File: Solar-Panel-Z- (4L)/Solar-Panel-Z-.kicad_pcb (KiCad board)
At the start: 4 copper layers, 48.4 x 48.4 mm, 81 parts, among them J1 FTS-105-01-L-DV-A, Q1 BSS138DWQ-7, Q2 MBT2222ADW1T1, Q3 BSS138DWQ-7, Q4 MBT2222ADW1T1, U1 BQ25570RGRR, U2 TSL2561

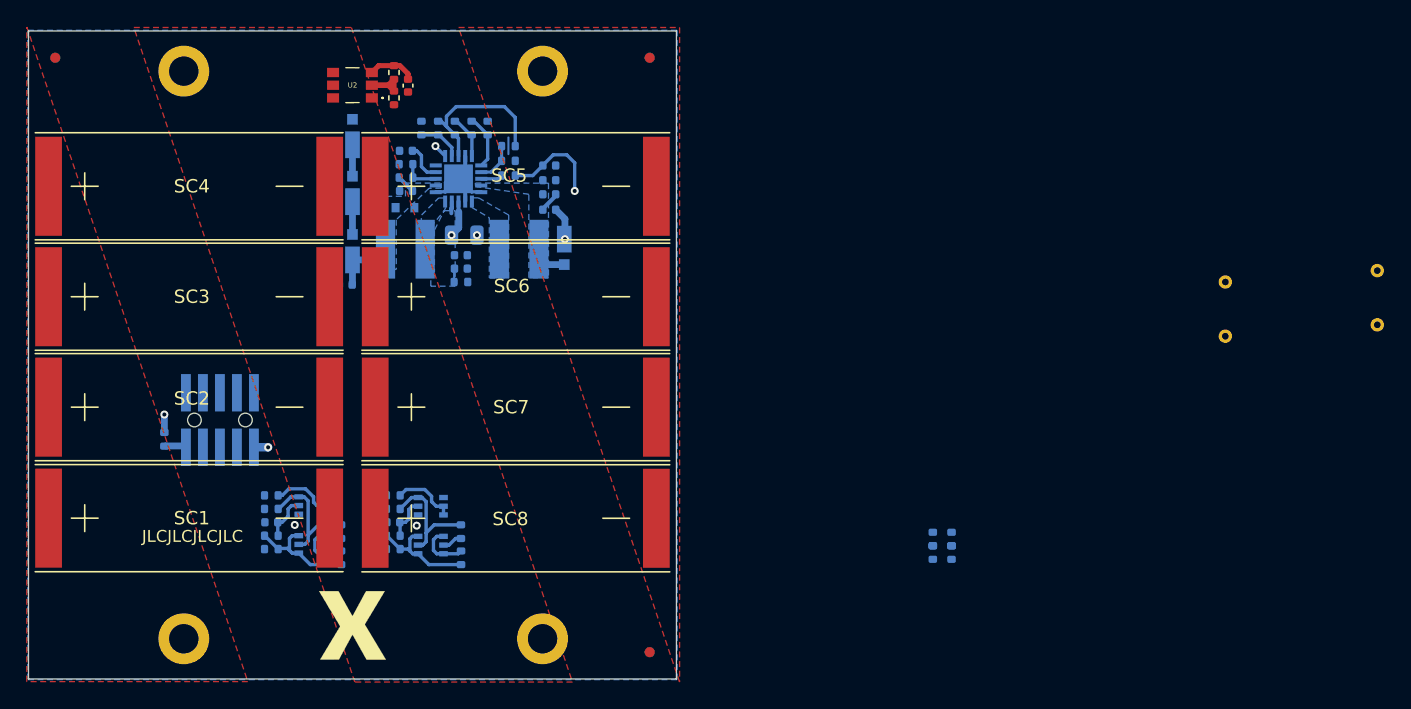
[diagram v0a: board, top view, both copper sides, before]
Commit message: Added 4 Layer Z- board
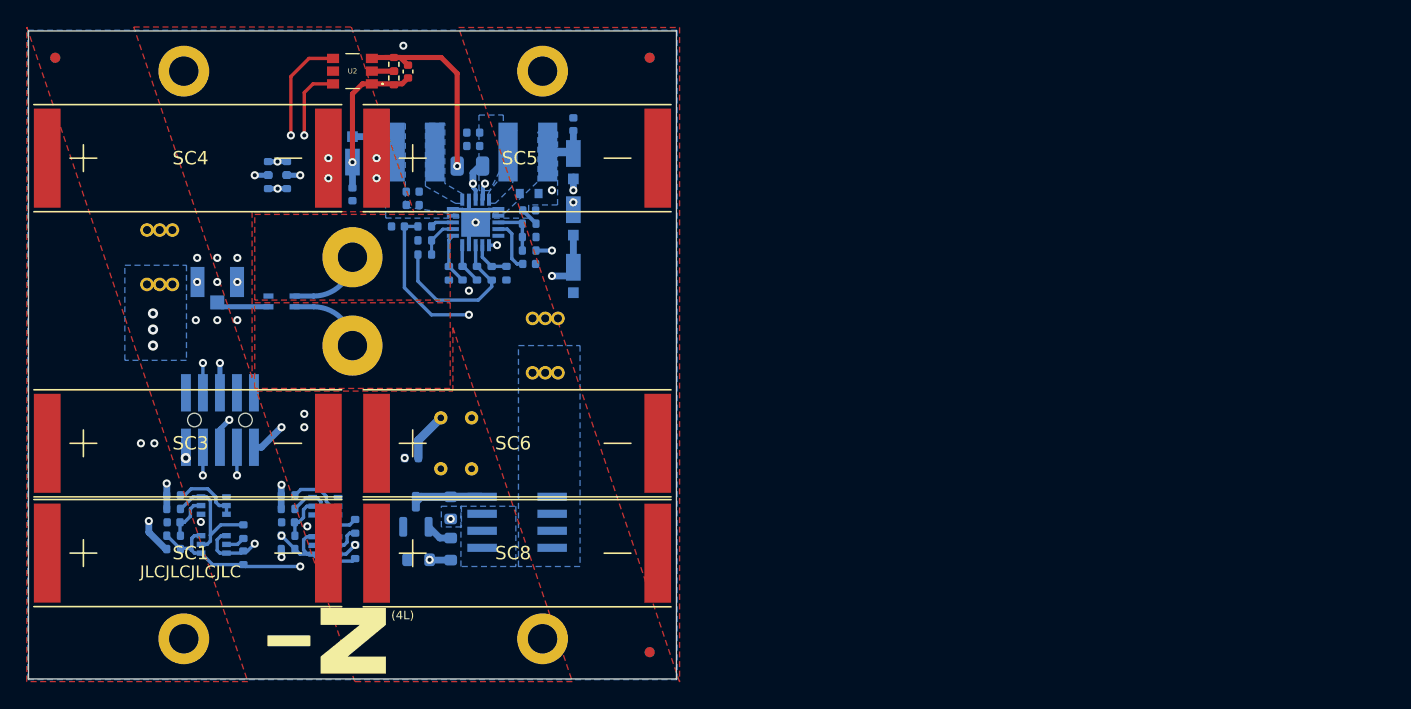
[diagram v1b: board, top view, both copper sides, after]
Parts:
- removed the REF** at (106.7, 88.2)
- removed SC2, SC7: SolarCell_Small, solarpanels:KXOB25-05X3F
- added H5: MountingHole_Pad, solarpanels:Antenna Pad, F.Cu at (106.7, 59.2)
- added H6: MountingHole_Pad, solarpanels:Antenna Pad, F.Cu at (106.7, 65.8)
- added J2: U.FL-R-SMT-1, solarpanels:U.FL-R-SMT-1, B.Cu at (96.6, 61.0)
- added JP1: Jumper, solarpanels:Burn-Wire-Rotated, B.Cu at (92.3, 59.2)
- added JP2: Jumper, solarpanels:Burn-Wire-Rotated, B.Cu at (121.1, 65.8)
- added Q5: IRLML2803, Package_TO_SOT_SMD:SOT-23, B.Cu at (111.4, 78.4)
- added R32: 4.7k, Resistor_SMD:R_0603_1608Metric, B.Cu at (114.0, 81.0)
- added R33: 100k, Resistor_SMD:R_0603_1608Metric, B.Cu at (114.0, 77.9)
- added R4: 10k, Resistor_SMD:R_0603_1608Metric, B.Cu at (111.6, 81.8)
- added Ref**: Val**, custom-footprints:ypanel, F.Cu at (106.1, 87.6)
- added U3: ATB2012-50011-T000, solarpanels:ATB2012, B.Cu at (101.4, 62.5)
- added U4: NDS8434, solarpanels:NDS8434, B.Cu at (119.0, 79.0)
- moved TP4 70.3 mm to (113.3, 71.2)
- moved TP3 69.3 mm to (115.6, 75.0)
- moved TP2 59.4 mm to (113.3, 75.0)
- moved TP1 57.2 mm to (115.6, 71.2)
- moved R13 56.8 mm to (101.8, 53.6)
- moved R17 56.8 mm to (100.4, 52.6)
- moved R18 56.8 mm to (100.4, 53.6)
- moved R12 56.8 mm to (101.8, 52.6)
- moved C2 20.8 mm to (123.2, 49.3), turned to 90 degrees
- moved D3 19.5 mm to (123.2, 60.6), turned to -90 degrees
- moved R3 18.5 mm to (111.1, 74.2), turned to 0 degrees
- moved D5 17.8 mm to (123.2, 52.1), turned to -90 degrees
- moved D2 17.3 mm to (106.7, 51.4), turned to 90 degrees
- moved D4 16.6 mm to (123.2, 56.3), turned to -90 degrees
- moved C11 14.7 mm to (106.7, 54.5), turned to -90 degrees
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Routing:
- net /coil: track 0.00 -> 6601.0 mm, vias 0 -> 3
- net SDA_LS: track 8.29 -> 63.8 mm, vias 0 -> 2
- net /VSOLAR_FULL: track 2.45 -> 50.4 mm, vias 0 -> 4
- net SCL_LS: track 8.04 -> 49.2 mm, vias 0 -> 2
- net Net-(D3-Pad1): track 2.35 -> 42.9 mm, vias 0 -> 7
- net /VBURN: track 0.00 -> 35.5 mm, vias 0 -> 3
- net BATT_P: track 1.47 -> 26.0 mm, vias 0 -> 3
- net SCL2: track 3.90 -> 28.0 mm, vias 0 -> 2
- net COIL_P: track 0.00 -> 23.8 mm, vias 0 -> 2
- net BURN1: track 0.00 -> 21.1 mm, vias 0 -> 2
- net VBAT: track 4.08 -> 25.0 mm, vias 2 -> 1
- net COIL_N: track 0.00 -> 18.3 mm, vias 0 -> 2
- net +3V3: track 3.55 -> 21.3 mm, vias 2 -> 6
- net VSOLAR: track 6.54 -> 24.3 mm, vias 0 -> 1
- net SDA2: track 3.73 -> 13.6 mm, vias 0 -> 2
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- added copper zone on B.Cu, net /VBURN
- added copper zone on B.Cu, net BATT_P
- added copper zone on In2.Cu, net GND
- added copper zone on F.Cu, net Net-(H5-Pad1)
- added copper zone on F.Cu, net Net-(H6-Pad1)
- removed copper zone on In2.Cu, net +3V3
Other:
- board text added: "(4L)"
- board text added: "v02"
- board text removed: "v04"

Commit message: Z board updates
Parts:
- moved R3 9.62 mm to (120.4, 71.7), turned to 90 degrees
- moved J2 8.35 mm to (102.1, 67.3), turned to 90 degrees
- moved TP1 2.30 mm to (113.3, 71.2)
- moved TP4 2.30 mm to (115.6, 71.2)
- moved JP1 1.30 mm to (92.3, 60.5)
- moved JP2 1.30 mm to (121.1, 64.5)
- moved D3 0.27 mm to (123.2, 60.3)
- moved U3 0.17 mm to (101.6, 62.5)
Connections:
- net SCL2 renamed SCL
- net SDA2 renamed SDA
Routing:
- net BATT_P: track 26.0 -> 33.9 mm
- net GND: track 22.0 -> 14.4 mm, vias 14 -> 6
- net VSOLAR: track 24.3 -> 31.1 mm
- net VBAT: track 25.0 -> 28.2 mm
- net /VBURN: track 35.5 -> 32.4 mm, vias 3 -> 0
- net SDA_LS: track 63.8 -> 61.1 mm
- net Net-(D3-Pad1): track 42.9 -> 40.3 mm, vias 7 -> 5
- net COIL_P: track 23.8 -> 25.1 mm
- net SCL_LS: track 49.2 -> 48.0 mm
- net Net-(J2-Pad3): track 3.50 -> 4.39 mm

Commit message: Exported Gerbers
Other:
- board text added: "08-AUG-2022"
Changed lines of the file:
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@@
       (drillshape 0)
       (scaleselection 1)
-      (outputdirectory "../../Z- (4L)/")
+      (outputdirectory "../gerbers/Gerbers Z- (4L) (08-08-2022)/")
     )
   )
@@
     (effects (font (size 1.143 1.143) (thickness 0.2032)) (justify mirror))
   )
+  (gr_text "08-AUG-2022" (at 112.4204 85.4202) (layer "B.SilkS")
+    (effects (font (size 0.508 0.508) (thickness 0.1016)) (justify mirror))
+  )
   (gr_text "Cable Pinout\n1.BATT_P\n2.VUSB\n3.BURN1\n4.BURN2\n5.COIL_P\n6.COIL_N\n7.SDA\n8.SCL\n9.+3V3\n10.GND" (at 90.45 71.15) (layer "B.SilkS")
     (effects (font (size 0.635 0.635) (thickness 0.0762)) (justify left mirror))
@@
   (segment (start 116.3213 77.095) (end 114.0425 77.095) (width 0.6096) (layer "B.Cu") (net 46))
   (zone (net 42) (net_name "Net-(H6-Pad1)") (layer "F.Cu") (hatch edge 0.508)
-    (connect_pads yes (clearance 0))
+    (connect_pads yes (clearance 0.1524))
     (min_thickness 0.254) (filled_areas_thickness no)
     (fill yes (thermal_gap 0.508) (thermal_bridge_width 0.508))
@@
   )
   (zone (net 41) (net_name "Net-(H5-Pad1)") (layer "F.Cu") (hatch edge 0.508)
-    (connect_pads yes (clearance 0))
+    (connect_pads yes (clearance 0.1524))
     (min_thickness 0.254) (filled_areas_thickness no)
     (fill yes (thermal_gap 0.508) (thermal_bridge_width 0.508))
@@
   )
   (zone (net 23) (net_name "/VSOLAR_FULL") (layer "F.Cu") (hatch edge 0.508)
-    (connect_pads yes (clearance 0.127))
+    (connect_pads yes (clearance 0.1524))
     (min_thickness 0.254) (filled_areas_thickness no)
     (fill yes (thermal_gap 0.508) (thermal_bridge_width 0.508))
@@
   )
   (zone (net 1) (net_name "GND") (layer "F.Cu") (hatch edge 0.508)
-    (connect_pads yes (clearance 0.127))
+    (connect_pads yes (clearance 0.1524))
     (min_thickness 0.254) (filled_areas_thickness no)
     (fill yes (thermal_gap 0.508) (thermal_bridge_width 0.508))
@@
   )
   (zone (net 26) (net_name "Net-(D3-Pad1)") (layer "F.Cu") (hatch edge 0.508)
-    (connect_pads yes (clearance 0.127))
+    (connect_pads yes (clearance 0.1524))
     (min_thickness 0.254) (filled_areas_thickness no)
     (fill yes (thermal_gap 0.508) (thermal_bridge_width 0.508))
@@
   (zone (net 6) (net_name "VSOLAR") (layer "B.Cu") (hatch edge 0.508)
     (priority 4)
-    (connect_pads yes (clearance 0.127))
-    (min_thickness 0.127) (filled_areas_thickness no)
-    (fill yes (thermal_gap 0.127) (thermal_bridge_width 0.2286))
+    (connect_pads yes (clearance 0.1524))
+    (min_thickness 0.254) (filled_areas_thickness no)
+    (fill yes (thermal_gap 0.254) (thermal_bridge_width 0.254))
     (polygon
       (pts
@@
   (zone (net 13) (net_name "Net-(C10-Pad1)") (layer "B.Cu") (hatch edge 0.508)
     (priority 6)
-    (connect_pads yes (clearance 0.127))
-    (min_thickness 0.127) (filled_areas_thickness no)
-    (fill yes (thermal_gap 0.127) (thermal_bridge_width 0.2286))
+    (connect_pads yes (clearance 0.1524))
+    (min_thickness 0.254) (filled_areas_thickness no)
+    (fill yes (thermal_gap 0.254) (thermal_bridge_width 0.254))
     (polygon
       (pts
@@
   (zone (net 14) (net_name "Net-(L2-Pad1)") (layer "B.Cu") (hatch edge 0.508)
     (priority 4)
-    (connect_pads yes (clearance 0.000001))
-    (min_thickness 0.2032) (filled_areas_thickness no)
+    (connect_pads yes (clearance 0.1524))
+    (min_thickness 0.254) (filled_areas_thickness no)
     (fill yes (thermal_gap 0.508) (thermal_bridge_width 0.508))
     (polygon
@@
   (zone (net 4) (net_name "Net-(L1-Pad2)") (layer "B.Cu") (hatch edge 0.508)
     (priority 6)
-    (connect_pads yes (clearance 0.000001))
-    (min_thickness 0.2032) (filled_areas_thickness no)
+    (connect_pads yes (clearance 0.1524))
+    (min_thickness 0.254) (filled_areas_thickness no)
     (fill yes (thermal_gap 0.508) (thermal_bridge_width 0.508))
     (polygon
@@
         (xy 116.8452 55.166656)
         (xy 116.8452 54.4664)
-        (xy 117.70116 52.753656)
-        (xy 117.70116 49.642156)
-        (xy 118.97116 49.642156)
-        (xy 118.65366 53.896656)
+        (xy 117.6274 53.4924)
+        (xy 117.6274 49.657)
+        (xy 118.99656 49.64214)
+        (xy 118.999 53.543184)
         (xy 117.38366 55.166656)
       )
@@
   (zone (net 3) (net_name "Net-(C7-Pad1)") (layer "B.Cu") (hatch edge 0.508)
     (priority 4)
-    (connect_pads yes (clearance 0.127))
-    (min_thickness 0.127) (filled_areas_thickness no)
-    (fill yes (thermal_gap 0.127) (thermal_bridge_width 0.2286))
+    (connect_pads yes (clearance 0.1524))
+    (min_thickness 0.254) (filled_areas_thickness no)
+    (fill yes (thermal_gap 0.254) (thermal_bridge_width 0.254))
     (polygon
       (pts
@@
         (xy 116.148414 48.581947)
         (xy 117.969624 48.574103)
-        (xy 117.97121 53.000244)
-        (xy 116.97044 54.219444)
-        (xy 116.15 54.219444)
+        (xy 118.026473 53.045606)
+        (xy 116.9924 54.2798)
+        (xy 116.1542 54.2798)
       )
     )
@@
   (zone (net 9) (net_name "BATT_P") (layer "B.Cu") (hatch edge 0.508)
     (priority 2)
-    (connect_pads yes (clearance 0.127))
+    (connect_pads yes (clearance 0.1524))
     (min_thickness 0.254) (filled_areas_thickness no)
     (fill yes (thermal_gap 0.508) (thermal_bridge_width 0.508))
@@
   (zone (net 44) (net_name "/VBURN") (layer "B.Cu") (hatch edge 0.508)
     (priority 2)
-    (connect_pads yes (clearance 0.127))
+    (connect_pads yes (clearance 0.1524))
     (min_thickness 0.254) (filled_areas_thickness no)
     (fill yes (thermal_gap 0.508) (thermal_bridge_width 0.508))
@@
   (zone (net 44) (net_name "/VBURN") (layer "B.Cu") (hatch edge 0.508)
     (priority 2)
-    (connect_pads yes (clearance 0.127))
+    (connect_pads yes (clearance 0.1524))
     (min_thickness 0.254) (filled_areas_thickness no)
     (fill yes (thermal_gap 0.508) (thermal_bridge_width 0.508))
@@
   )
   (zone (net 1) (net_name "GND") (layers "In2.Cu" "B.Cu") (hatch edge 0.508)
-    (connect_pads yes (clearance 0))
+    (connect_pads yes (clearance 0.1524))
     (min_thickness 0.254) (filled_areas_thickness no)
     (fill yes (thermal_gap 0.254) (thermal_bridge_width 0.254))

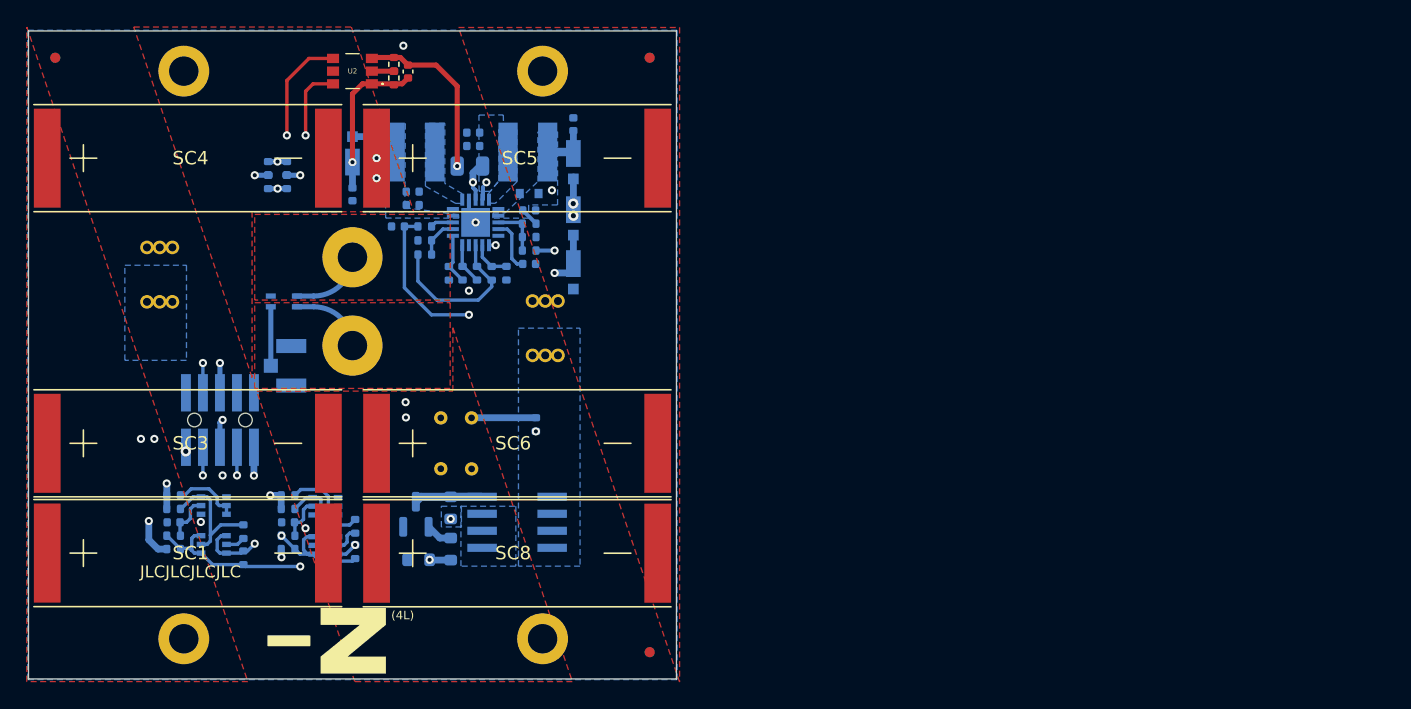
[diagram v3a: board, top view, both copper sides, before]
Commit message: Z- board antenna updates
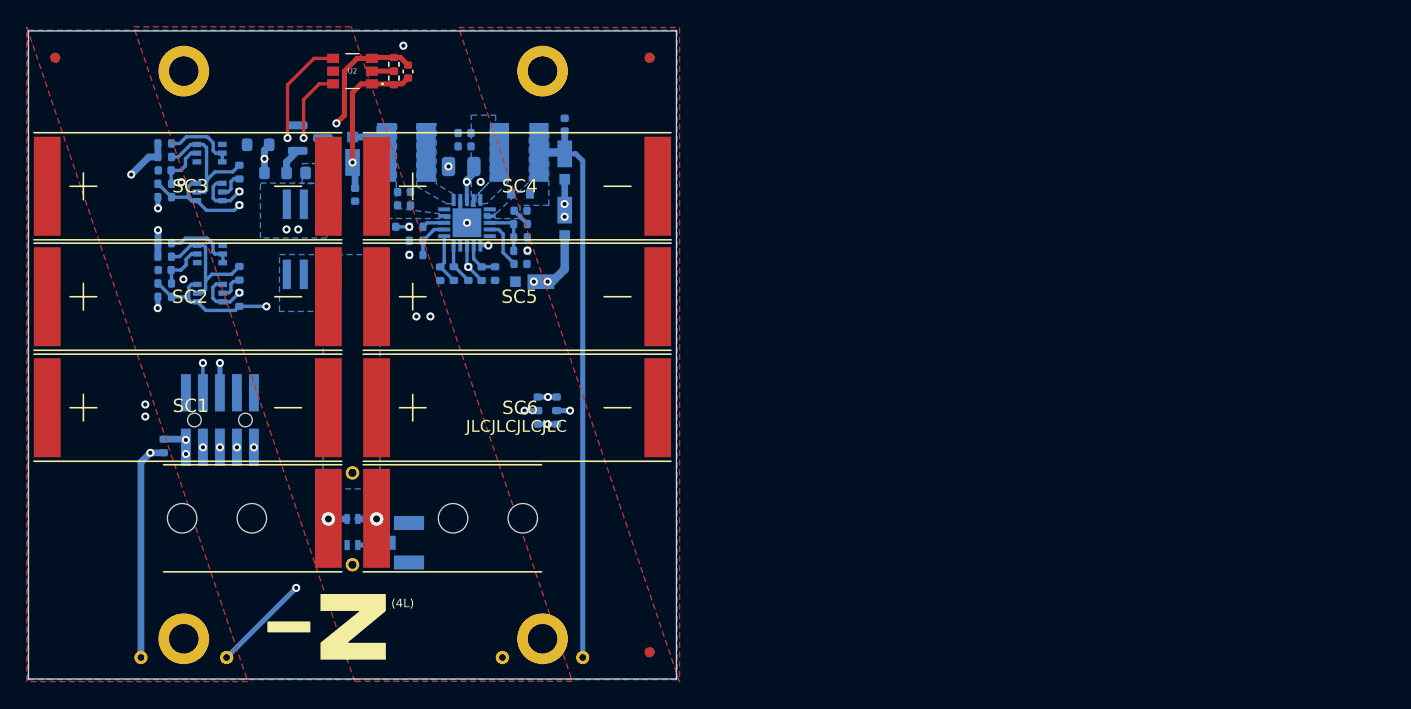
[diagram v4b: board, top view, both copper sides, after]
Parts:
- removed JP2: Jumper, solarpanels:Burn-Wire-Rotated
- H5, H6: footprint solarpanels:Antenna Pad -> solarpanels:Antenna Mount
- moved R4 33.2 mm to (99.7, 50.8)
- moved R32 31.0 mm to (101.0, 52.9), turned to 180 degrees
- moved TP4 30.5 mm to (90.9, 89.1)
- moved Q5 29.2 mm to (103.5, 50.3), turned to 0 degrees
- moved R3 27.8 mm to (92.6, 73.3), turned to -90 degrees
- moved R33 27.0 mm to (104.0, 52.9), turned to 180 degrees
- moved R27 26.9 mm to (98.2, 52.8)
- moved R23 26.9 mm to (98.2, 54.8)
- moved R13 26.8 mm to (122.0, 71.2)
- moved R18 26.7 mm to (120.5, 71.2)
- moved R12 26.7 mm to (122.0, 70.2)
- moved R17 26.7 mm to (120.5, 70.2)
- moved Q3 26.3 mm to (96.0, 51.4)
- moved Q4 26.3 mm to (96.0, 54.3)
- moved C13 26.3 mm to (92.7, 52.7)
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- renumbered SC3 to SC2, SC4 to SC3, SC5 to SC4, SC6 to SC5, SC8 to SC6
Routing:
- net /coil: track 6601.0 -> 6062.2 mm
- net SDA_LS: track 61.1 -> 22.5 mm
- net /VBURN: track 32.4 -> 0.00 mm
- net VBAT: track 28.2 -> 60.1 mm, vias 1 -> 2
- net Net-(D3-Pad1): track 40.3 -> 15.6 mm, vias 5 -> 4
- net SCL_LS: track 48.0 -> 32.3 mm
- net SCL: track 28.1 -> 13.3 mm
- net VSOLAR: track 31.1 -> 43.5 mm, vias 1 -> 0
- net SDA: track 13.6 -> 25.8 mm
- net VOUT_EN: track 17.8 -> 8.09 mm
- net COIL_N: track 18.3 -> 27.8 mm
- net +3V3: track 21.1 -> 26.4 mm, vias 6 -> 7
- net BURN1: track 20.6 -> 25.3 mm
- net Net-(H6-Pad1): track 5.86 -> 1.40 mm, vias 0 -> 1
- net Net-(H5-Pad1): track 5.86 -> 1.40 mm, vias 0 -> 1
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- removed copper zone on F.Cu, net Net-(H5-Pad1)
- removed copper zone on F.Cu, net Net-(H6-Pad1)
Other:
- board text added: "1.+3V3 3.BURN1 5.COIL_P 7.SDA 9.BATT_P"
- board text added: "2.GND 4.BURN2 6.COIL_N 8.SCL 10.VUSB"
- board text added: "Rev B/02"
- board text removed: "08-AUG-2022"
- board text removed: "Cable Pinout 1.BATT_P 2.VUSB 3.BURN1 4.BURN2 5.COIL_P 6.COIL_N 7.SDA 8.SCL 9.+3V3 10.GND"
- board text removed: "v02"
